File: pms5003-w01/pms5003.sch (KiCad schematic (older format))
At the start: 23 parts, among them J1 Battery, J2 DS3231, J3 PMS5003, J4 SHT10, J5 P2, J6 PROG, J7 USB_OTG, Q1 IRF540N, Q2 IRF7309IPBF, U1 U3V12F5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

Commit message: Add W01-based PMS5003 board
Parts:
- removed U11: LoPy4, Pycom:LoPy_with_headers, symbol LoPy4
- added AE1: Antenna, various:Rainsun_AN9520, symbol Antenna
- added C3: 1u, Capacitors_Tantalum_SMD:CP_Tantalum_Case-A_EIA-3216-18_Reflow, symbol CP
- added C4: 100u, Capacitors_SMD:CP_Elec_6.3x7.7, symbol CP
- added C5: 100n, Capacitors_SMD:C_1206, symbol C
- added U11: W01, Pycom:W01, symbol W01
- added U3: TC1262-33, TO_SOT_Packages_SMD:TO-263-3_TabPin2, symbol TC1262-33
- J3: footprint Socket_Strips:Socket_Strip_Angled_1x06_Pitch2.54mm -> Socket_Strips:Socket_Strip_Straight_1x06_Pitch2.54mm; 1st Distrib Link (none) -> Value; 1st Distrib PN (none) -> Value; 2nd Distrib Link (none) -> Value; 2nd Distrib PN (none) -> Value; MFG Name (none) -> Value; MFG Part Num (none) -> Value
- J4: footprint Socket_Strips:Socket_Strip_Angled_1x04_Pitch2.54mm -> Pin_Headers:Pin_Header_Straight_1x04_Pitch2.54mm; 1st Distrib Link (none) -> Value; 1st Distrib PN (none) -> Value; 2nd Distrib Link (none) -> Value; 2nd Distrib PN (none) -> Value; MFG Name (none) -> Value; MFG Part Num (none) -> Value
- J7: footprint Connectors:USB_Micro-B -> Connectors_USB:USB_Micro-B_Molex_47346-0001; 1st Distrib Link (none) -> Value; 1st Distrib PN (none) -> Value; 2nd Distrib Link (none) -> Value; 2nd Distrib PN (none) -> Value; MFG Name (none) -> Value; MFG Part Num (none) -> Value
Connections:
- wire segments 134 -> 145
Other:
- moved on the sheet: Q2A, R4, R5

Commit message: Next iteration of w01 pms5003
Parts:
- removed AE1: Antenna, various:Rainsun_AN9520, symbol Antenna
- added AE1: Antenna_Shield, Connector_Coaxial:U.FL_Molex_MCRF_73412-0110_Vertical, symbol Antenna_Shield
- added C6: 22pF, Capacitors_SMD:C_0805, symbol C
- added C7: 1nF, Capacitors_SMD:C_0805, symbol C
- added R7: 10k, Resistors_SMD:R_1206, symbol R
- added SW1: SW_Push, Buttons_Switches_SMD:SW_SPST_B3S-1000, symbol SW_Push
- J2: footprint Socket_Strips:Socket_Strip_Straight_1x05_Pitch2.54mm -> various:DS3231; 1st Distrib Link (none) -> Value; 1st Distrib PN (none) -> Value; 2nd Distrib Link (none) -> Value; 2nd Distrib PN (none) -> Value; MFG Name (none) -> Value; MFG Part Num (none) -> Value
- J5: footprint Socket_Strips:Socket_Strip_Straight_1x02_Pitch2.54mm -> Pin_Headers:Pin_Header_Straight_1x02_Pitch2.54mm; 1st Distrib Link (none) -> Value; 1st Distrib PN (none) -> Value; 2nd Distrib Link (none) -> Value; 2nd Distrib PN (none) -> Value; MFG Name (none) -> Value; MFG Part Num (none) -> Value
- J7: footprint Connectors_USB:USB_Micro-B_Molex_47346-0001 -> various:USB_Micro-B_91-US01-517
- R2: value 100 -> 470
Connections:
- net 3V3: now also R7.1
- net GND: now also AE1.2 (Shield), C7.2, SW1.1
- net at U11.16 (ESP_ANT): now also C6.1
- net RST: now reaches U11.2 (Reset)
- net RST: now also C7.1, R7.2, SW1.2
- new net: AE1.1 (A), C6.2
- no-connect marks 17 -> 16
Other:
- moved on the sheet: C1, C2, C3, C4, C5, D1, D2, D3, J1, J2, J3, J4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

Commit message: W01 placement
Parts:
- added R?: 100, symbol R
- J7: symbol USB_OTG -> USB_OTG-RESCUE-pms5003
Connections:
- net 3V3: now also R?.1; no longer J2.1 (VCC), J4.4 (VCC)
- net PMS_EN: now also U11.7 (P4); no longer U11.23 (P19)
- new net SHT_RTC_VCC: J2.1 (VCC), J4.4 (VCC), R?.2, U11.23 (P19)

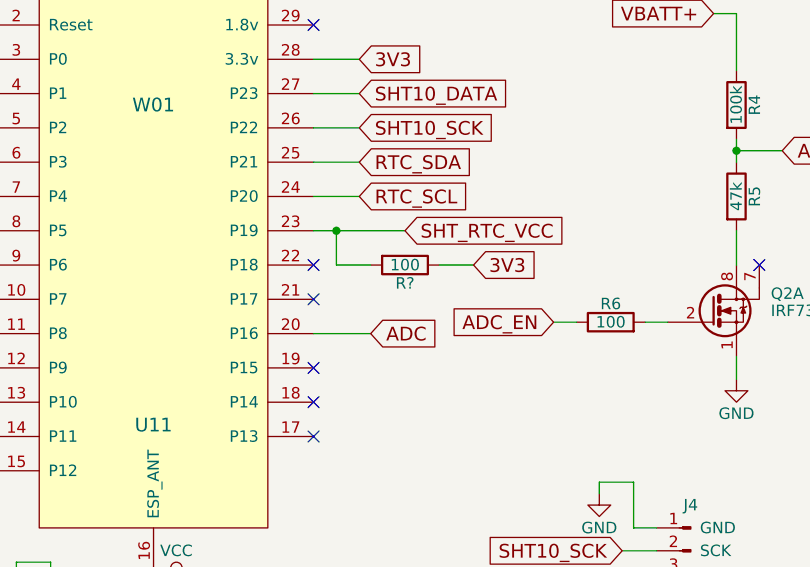
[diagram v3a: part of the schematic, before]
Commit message: Release PMS5003 in two versions
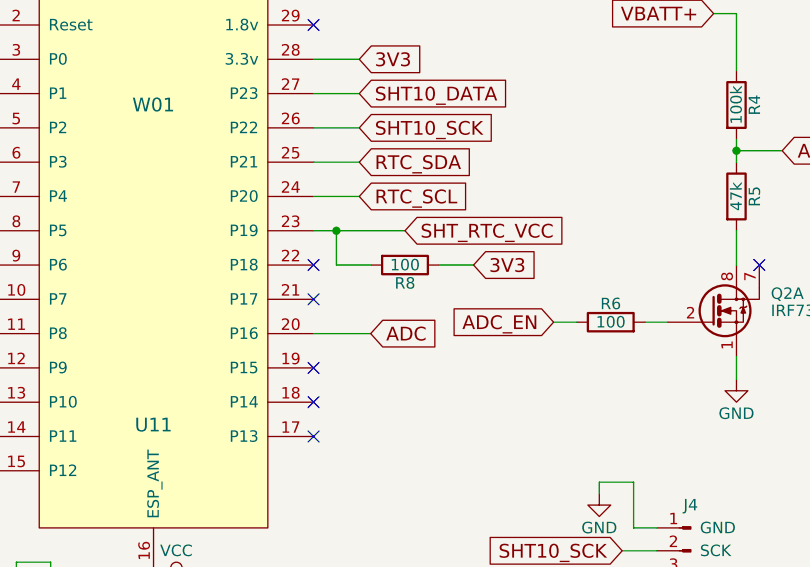
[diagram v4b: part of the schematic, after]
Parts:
- gave numbers to parts that had none: 1
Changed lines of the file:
@@
 3V3
 $Comp
-L R R?
+L R R8
 U 1 1 5A6A7E1C
 P 4900 2100
-F 0 "R?" V 4980 2100 50  0000 C CNN
+F 0 "R8" V 4980 2100 50  0000 C CNN
 F 1 "100" V 4900 2100 50  0000 C CNN
 F 2 "" V 4830 2100 50  0001 C CNN

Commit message: Update footprint for W01's voltage regulator
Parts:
- U3: footprint TO_SOT_Packages_SMD:TO-263-3_TabPin2 -> TO_SOT_Packages_SMD:SOT-223-3_TabPin2
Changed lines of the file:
@@
 F 0 "U3" H 7700 1675 50  0000 C CNN
 F 1 "TC1262-33" H 7850 1675 50  0000 L CNN
-F 2 "TO_SOT_Packages_SMD:TO-263-3_TabPin2" H 7850 1775 50  0001 C CIN
+F 2 "TO_SOT_Packages_SMD:SOT-223-3_TabPin2" H 7850 1775 50  0001 C CIN
 F 3 "" H 7850 1250 50  0001 C CNN
 F 4 "Value" H 7850 1550 60  0001 C CNN "MFG Name"
